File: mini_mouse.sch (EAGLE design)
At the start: 18 parts, among them IC1 PIC18F4550_TQFP

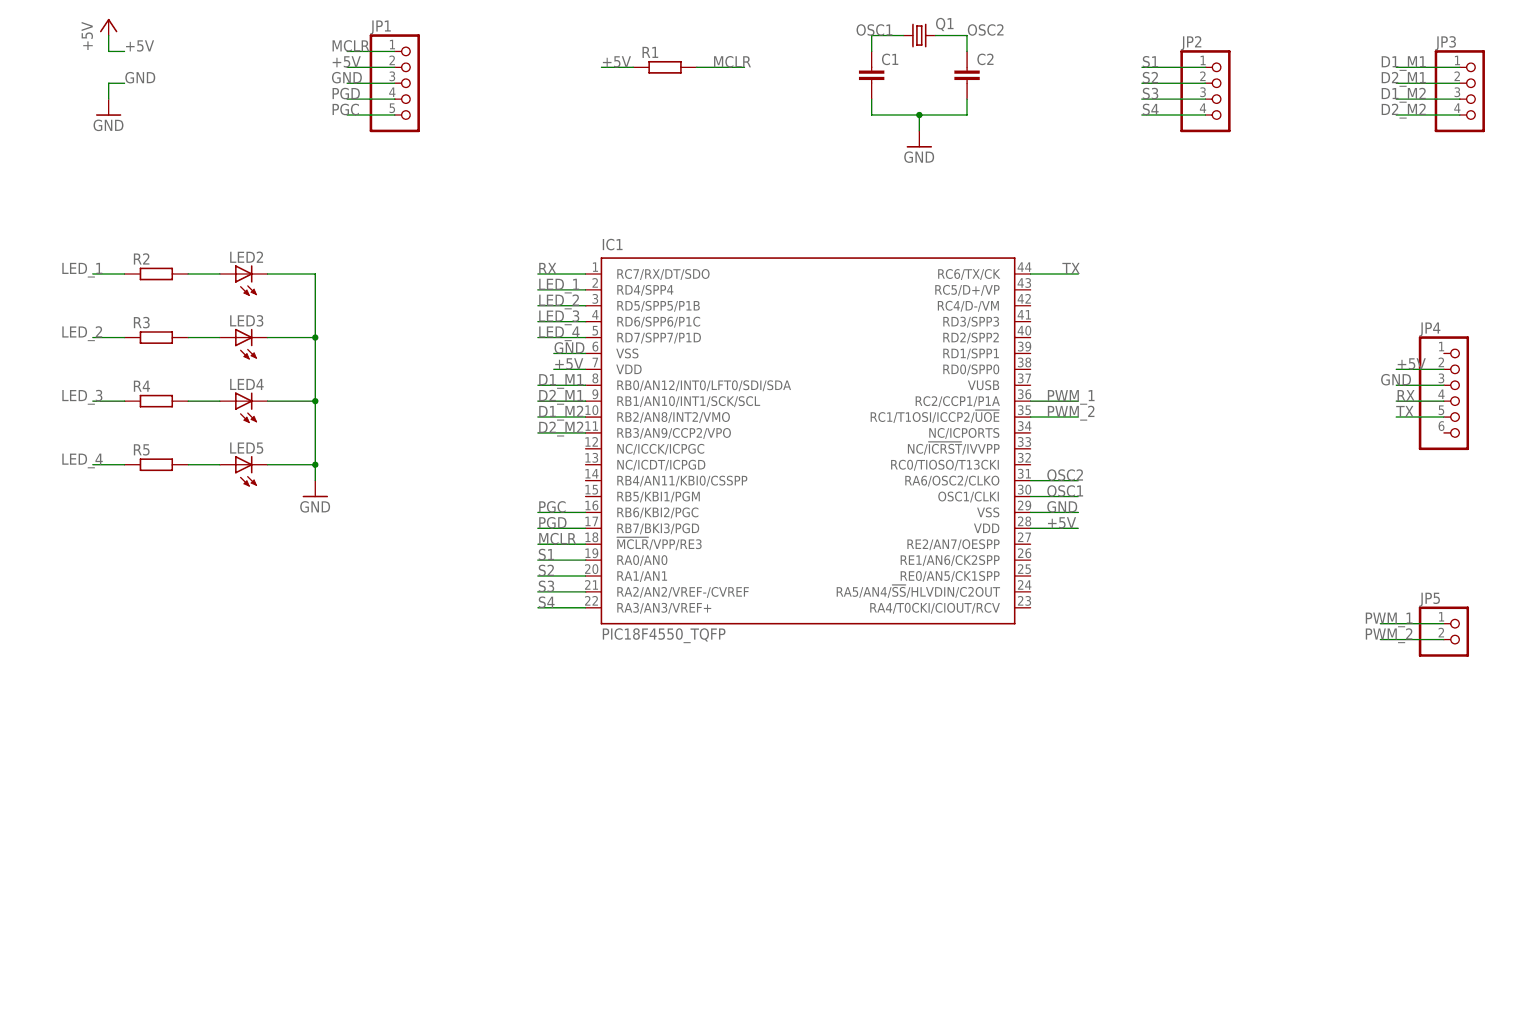
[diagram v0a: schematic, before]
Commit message: Componentes agregados
Encoder, puente h, switches, clemas alimentacion
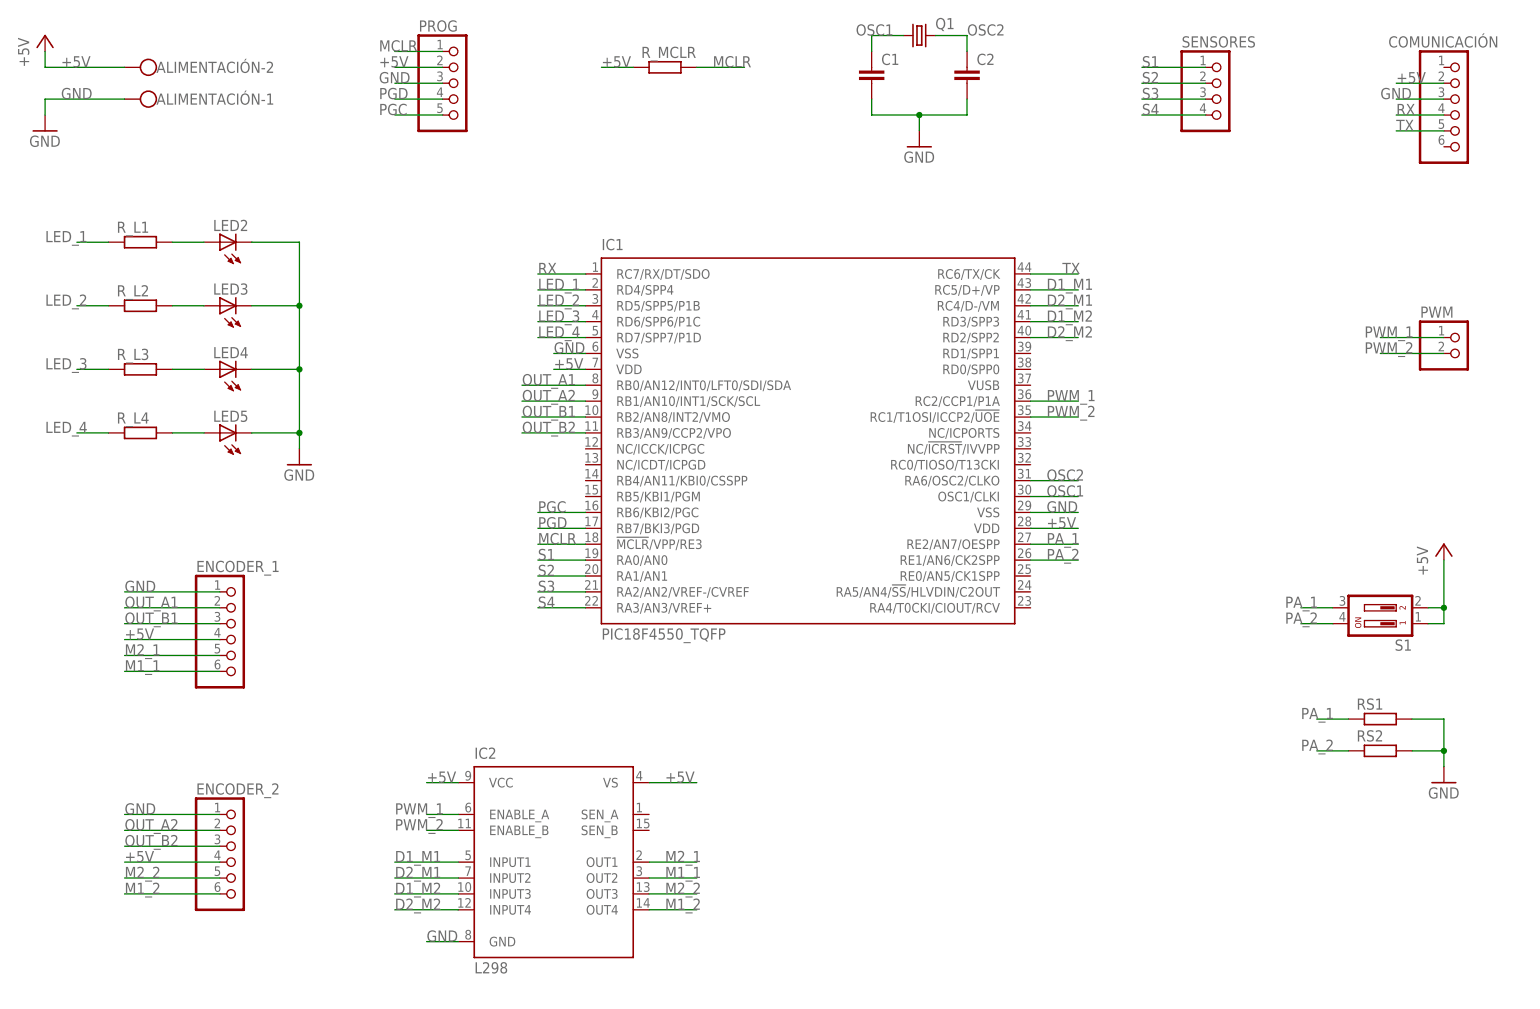
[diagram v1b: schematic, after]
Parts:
- removed JP1: (no value), pinhead:PINHD-1X5
- removed JP3: (no value), pinhead:PINHD-1X4
- removed JP4: (no value), pinhead:PINHD-1X6
- removed JP5: (no value), pinhead:PINHD-1X2
- removed R2, R3, R4, R5: (no value), rcl:R-EU_R0603
- added ALIMENTACIÓN: (no value), con-wago-500:W237-102
- added COMUNICACIÓN, ENCODER_1, ENCODER_2: (no value), pinhead:PINHD-1X6
- added IC2: L298, st-microelectronics:L298
- added PROG: (no value), pinhead:PINHD-1X5
- added PWM: (no value), pinhead:PINHD-1X2
- added RS1, RS2, R_L1, R_L2, R_L3, R_L4: (no value), rcl:R-EU_R0603
- added S1: (no value), switch-dil:DIP02YL
- renumbered JP2 to SENSORES, R1 to R_MCLR
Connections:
- new net M1_1: ENCODER_1.6, IC2.OUT2
- new net M1_2: ENCODER_2.6, IC2.OUT4
- new net M2_1: ENCODER_1.5, IC2.OUT1
- new net M2_2: ENCODER_2.5, IC2.OUT3
- new net OUT_A1: ENCODER_1.2, IC1.RB0/AN12/INT0/LFT0/SDI/SDA
- new net OUT_A2: ENCODER_2.2, IC1.RB1/AN10/INT1/SCK/SCL
- new net OUT_B1: ENCODER_1.3, IC1.RB2/AN8/INT2/VMO
- new net OUT_B2: ENCODER_2.3, IC1.RB3/AN9/CCP2/VPO
- new net PA_1: IC1.RE2/AN7/OESPP, RS1.1, S1.3
- new net PA_2: IC1.RE1/AN6/CK2SPP, RS2.1, S1.4
- net +5V: now also ALIMENTACIÓN-2.KL, COMUNICACIÓN.2, ENCODER_1.4, ENCODER_2.4, IC2.VCC, IC2.VS, PROG.2, S1.1, S1.2; no longer JP1.2, JP4.2
- net D1_M1: now also IC1.RC5/D+/VP, IC2.INPUT1; no longer IC1.RB0/AN12/INT0/LFT0/SDI/SDA, JP3.1
- net D1_M2: now also IC1.RD3/SPP3, IC2.INPUT3; no longer IC1.RB2/AN8/INT2/VMO, JP3.3
- net D2_M1: now also IC1.RC4/D-/VM, IC2.INPUT2; no longer IC1.RB1/AN10/INT1/SCK/SCL, JP3.2
- net D2_M2: now also IC1.RD2/SPP2, IC2.INPUT4; no longer IC1.RB3/AN9/CCP2/VPO, JP3.4
- net GND: now also ALIMENTACIÓN-1.KL, COMUNICACIÓN.3, ENCODER_1.1, ENCODER_2.1, IC2.GND, PROG.3, RS1.2, RS2.2; no longer JP1.3, JP4.3
- net LED_1: now also R_L1.1; no longer R2.1
- net LED_2: now also R_L2.1; no longer R3.1
- net LED_3: now also R_L3.1; no longer R4.1
- net LED_4: now also R_L4.1; no longer R5.1
- net MCLR: now also PROG.1; no longer JP1.1
- net N$1: now also R_L1.2; no longer R2.2
- net N$2: now also R_L2.2; no longer R3.2
- net N$3: now also R_L3.2; no longer R4.2
- net N$4: now also R_L4.2; no longer R5.2
- net PGC: now also PROG.5; no longer JP1.5
- net PGD: now also PROG.4; no longer JP1.4
- net PWM_1: now also IC2.ENABLE_A, PWM.1; no longer JP5.1
- net PWM_2: now also IC2.ENABLE_B, PWM.2; no longer JP5.2
- net RX: now also COMUNICACIÓN.4; no longer JP4.4
- net TX: now also COMUNICACIÓN.5; no longer JP4.5
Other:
- moved on the sheet: LED2, LED3, LED4, LED5

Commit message: Agregar regulador de voltaje
Se modificó el archivo para agregar un regulador de voltaje a 5V
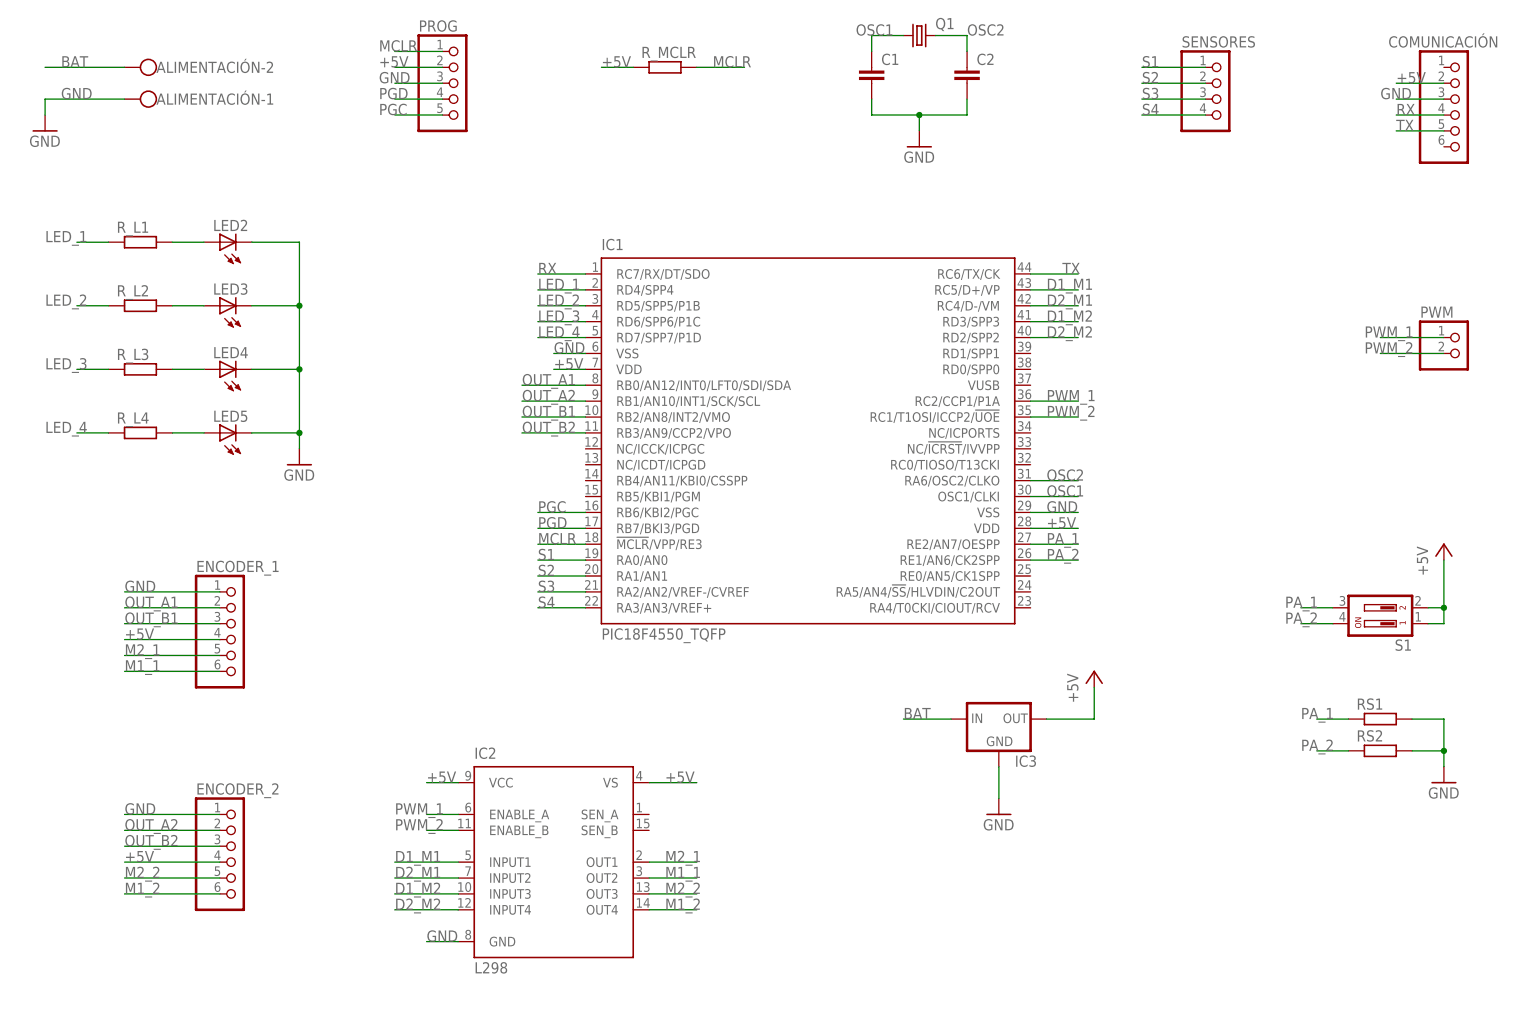
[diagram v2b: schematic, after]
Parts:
- added IC3: (no value), v-reg:78XXL
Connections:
- new net BAT: ALIMENTACIÓN-2.KL, IC3.IN
- net +5V: now also IC3.OUT; no longer ALIMENTACIÓN-2.KL
- net GND: now also IC3.GND
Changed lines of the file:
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@@
 <part name="R_MCLR" library="rcl" library_urn="urn:adsk.eagle:library:334" deviceset="R-EU_" device="R0603" package3d_urn="urn:adsk.eagle:package:23555/3"/>
 <part name="PROG" library="pinhead" library_urn="urn:adsk.eagle:library:325" deviceset="PINHD-1X5" device="" package3d_urn="urn:adsk.eagle:package:22469/2"/>
-<part name="P+1" library="supply1" library_urn="urn:adsk.eagle:library:371" deviceset="+5V" device=""/>
 <part name="GND1" library="supply1" library_urn="urn:adsk.eagle:library:371" deviceset="GND" device=""/>
 <part name="GND2" library="supply1" library_urn="urn:adsk.eagle:library:371" deviceset="GND" device=""/>
@@
 <part name="GND4" library="supply1" library_urn="urn:adsk.eagle:library:371" deviceset="GND" device=""/>
 <part name="P+2" library="supply1" library_urn="urn:adsk.eagle:library:371" deviceset="+5V" device=""/>
+<part name="IC3" library="v-reg" library_urn="urn:adsk.eagle:library:409" deviceset="78XXL" device="" package3d_urn="urn:adsk.eagle:package:30361/1"/>
+<part name="GND5" library="supply1" library_urn="urn:adsk.eagle:library:371" deviceset="GND" device=""/>
+<part name="P+1" library="supply1" library_urn="urn:adsk.eagle:library:371" deviceset="+5V" device=""/>
 </parts>
 <sheets>
@@
 <attribute name="VALUE" x="72.39" y="147.32" size="1.778" layer="96"/>
 </instance>
-<instance part="P+1" gate="1" x="12.7" y="165.1">
-<attribute name="VALUE" x="10.16" y="160.02" size="1.778" layer="96" rot="R90"/>
-</instance>
 <instance part="GND1" gate="1" x="12.7" y="149.86">
 <attribute name="VALUE" x="10.16" y="147.32" size="1.778" layer="96"/>
@@
 <instance part="P+2" gate="1" x="236.22" y="83.82">
 <attribute name="VALUE" x="233.68" y="78.74" size="1.778" layer="96" rot="R90"/>
+</instance>
+<instance part="IC3" gate="A" x="165.1" y="55.88">
+<attribute name="NAME" x="167.64" y="48.26" size="1.778" layer="95"/>
+<attribute name="VALUE" x="167.64" y="45.72" size="1.778" layer="96"/>
+</instance>
+<instance part="GND5" gate="1" x="165.1" y="40.64">
+<attribute name="VALUE" x="162.56" y="38.1" size="1.778" layer="96"/>
+</instance>
+<instance part="P+1" gate="1" x="180.34" y="63.5">
+<attribute name="VALUE" x="177.8" y="58.42" size="1.778" layer="96" rot="R90"/>
 </instance>
 </instances>
@@
 <wire x1="99.06" y1="111.76" x2="93.98" y2="111.76" width="0.1524" layer="91"/>
 <label x="93.98" y="111.76" size="1.778" layer="95"/>
-</segment>
-<segment>
-<pinref part="P+1" gate="1" pin="+5V"/>
-<wire x1="12.7" y1="162.56" x2="12.7" y2="160.02" width="0.1524" layer="91"/>
-<label x="15.24" y="160.02" size="1.778" layer="95"/>
-<pinref part="ALIMENTACIÓN" gate="-2" pin="KL"/>
-<wire x1="12.7" y1="160.02" x2="25.4" y2="160.02" width="0.1524" layer="91"/>
 </segment>
 <segment>
@@
 <wire x1="236.22" y1="81.28" x2="236.22" y2="73.66" width="0.1524" layer="91"/>
 <junction x="236.22" y="73.66"/>
+</segment>
+<segment>
+<pinref part="IC3" gate="A" pin="OUT"/>
+<wire x1="172.72" y1="55.88" x2="180.34" y2="55.88" width="0.1524" layer="91"/>
+<pinref part="P+1" gate="1" pin="+5V"/>
+<wire x1="180.34" y1="60.96" x2="180.34" y2="55.88" width="0.1524" layer="91"/>
 </segment>
 </net>
@@
 <junction x="236.22" y="50.8"/>
 </segment>
+<segment>
+<pinref part="IC3" gate="A" pin="GND"/>
+<wire x1="165.1" y1="48.26" x2="165.1" y2="43.18" width="0.1524" layer="91"/>
+<pinref part="GND5" gate="1" pin="GND"/>
+</segment>
 </net>
 <net name="OSC2" class="0">
@@
 </segment>
 </net>
+<net name="BAT" class="0">
+<segment>
+<label x="15.24" y="160.02" size="1.778" layer="95"/>
+<pinref part="ALIMENTACIÓN" gate="-2" pin="KL"/>
+<wire x1="12.7" y1="160.02" x2="25.4" y2="160.02" width="0.1524" layer="91"/>
+</segment>
+<segment>
+<pinref part="IC3" gate="A" pin="IN"/>
+<wire x1="157.48" y1="55.88" x2="149.86" y2="55.88" width="0.1524" layer="91"/>
+<label x="149.86" y="55.88" size="1.778" layer="95"/>
+</segment>
+</net>

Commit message: Cambios en componentes
Se cambiaron los empaquetados de algunos componentes como regulador de voltaje junto con sus capacitores. Se agregaron botones para las secuencias y on/off
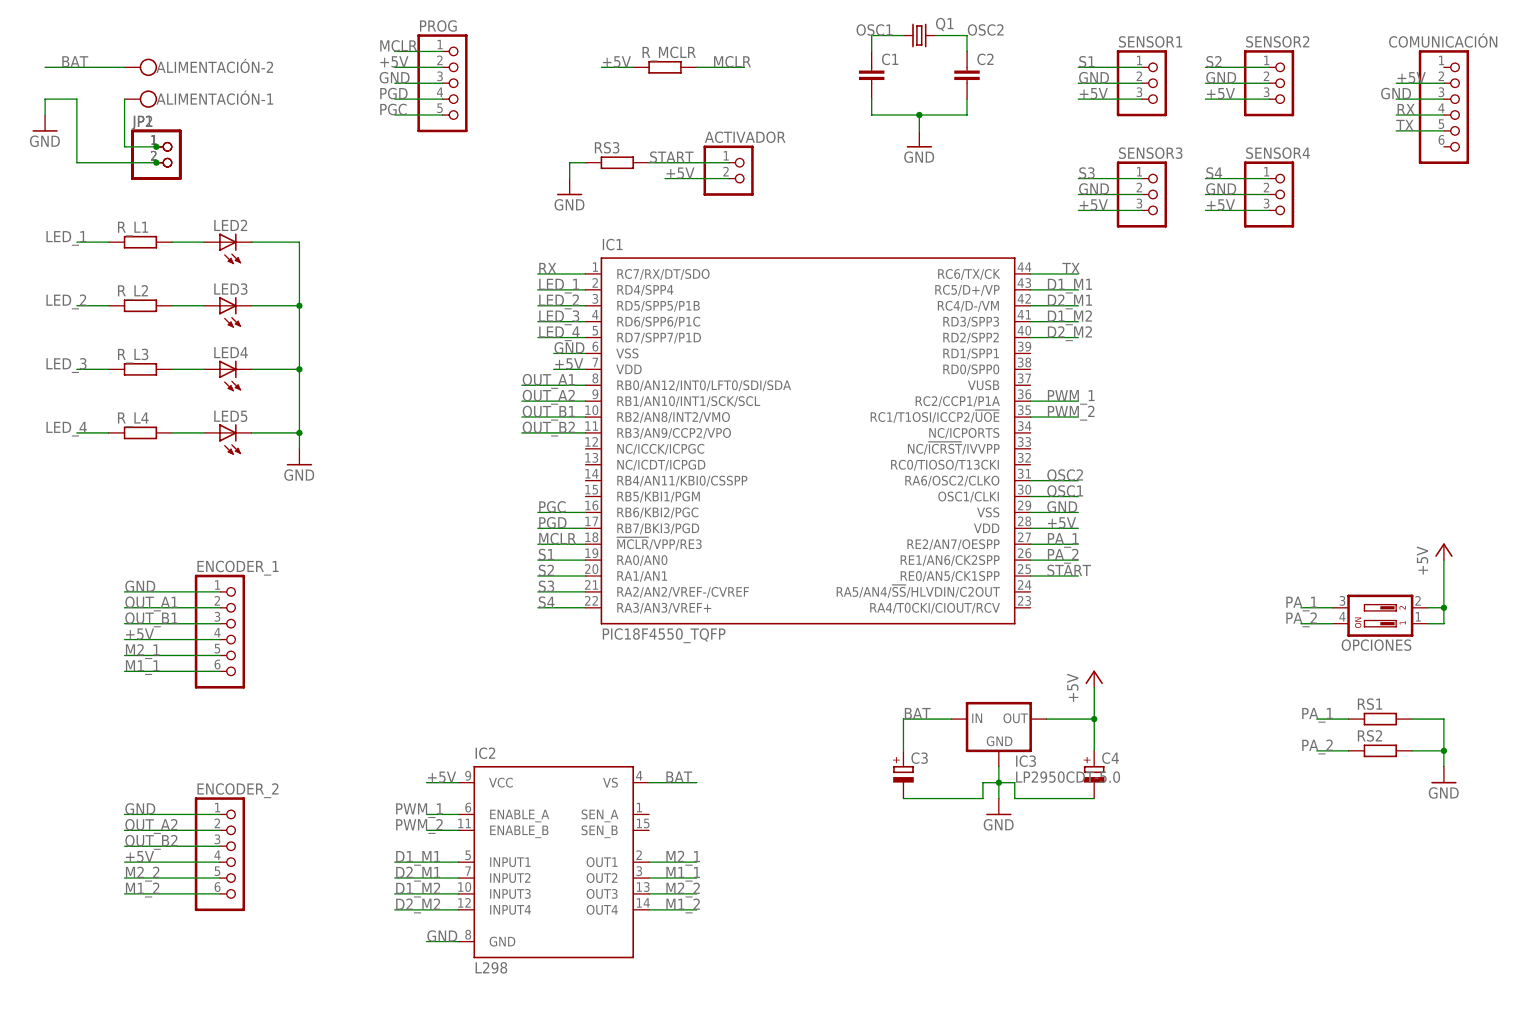
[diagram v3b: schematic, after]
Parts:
- removed PWM: (no value), pinhead:PINHD-1X2
- removed SENSORES: (no value), pinhead:PINHD-1X4
- added ACTIVADOR, JP1, JP2: (no value), pinhead:PINHD-1X2
- added C3, C4: (no value), rcl:CPOL-EU153CLV-0405
- added RS3: (no value), rcl:R-EU_R0603
- added SENSOR1, SENSOR2, SENSOR3, SENSOR4: (no value), pinhead:PINHD-1X3
- IC3: value (none) -> LP2950CDT-5.0; device v-reg:78XXL -> v-reg:LP2950CDT-5.0
- renumbered S1 to OPCIONES
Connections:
- new net N$5: ALIMENTACIÓN-1.KL, JP1.1, JP2.1
- new net START: ACTIVADOR.1, IC1.RE0/AN5/CK1SPP, RS3.2
- net +5V: now also ACTIVADOR.2, C4.+, SENSOR1.3, SENSOR2.3, SENSOR3.3, SENSOR4.3; no longer IC2.VS
- net BAT: now also C3.+, IC2.VS
- net GND: now also C3.-, C4.-, JP1.2, JP2.2, RS3.1, SENSOR1.2, SENSOR2.2, SENSOR3.2, SENSOR4.2; no longer ALIMENTACIÓN-1.KL
- net PWM_1: no longer PWM.1
- net PWM_2: no longer PWM.2
- net S1: now also SENSOR1.1; no longer SENSORES.1
- net S2: now also SENSOR2.1; no longer SENSORES.2
- net S3: now also SENSOR3.1; no longer SENSORES.3
- net S4: now also SENSOR4.1; no longer SENSORES.4
